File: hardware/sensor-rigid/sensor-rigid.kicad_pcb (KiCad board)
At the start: 4 copper layers, 28.5 x 21.7 mm, 27 parts, among them J1 Conn_01x05, U1 PCA9546APWR

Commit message: Interrupts and new flex design
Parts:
- moved R7 8.97 mm to (156.8, 51.8)
- moved R3 7.17 mm to (154.0, 54.2), turned to 180 degrees
- moved R13 7.07 mm to (160.5, 61.5)
- moved R9 7.00 mm to (160.8, 51.6), turned to 0 degrees
- moved JP4 6.35 mm to (163.1, 60.9)
- moved JP3 3.54 mm to (163.2, 58.4)
- moved R14 3.54 mm to (160.6, 58.5)
- moved R6 2.92 mm to (153.6, 51.8), turned to 0 degrees
- moved TP4 2.66 mm to (147.8, 63.8)
- moved R12 2.63 mm to (150.2, 61.4), turned to -90 degrees
- moved D1 2.26 mm to (139.6, 44.9)
- moved R4 2.26 mm to (138.8, 47.2)
- moved TP3 2.15 mm to (148.0, 57.8)
- moved R2 1.86 mm to (146.2, 60.6)
- moved U1 1.42 mm to (153.9, 58.9)
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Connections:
- net Net-(U1-SD0) renamed /SDA1
- net Net-(U1-SD1) renamed /SDA2
- D2 pad 3: Net-(D2-COM) -> /INT1
- D3 pad 3: Net-(D3-COM) -> /INT2
- FPC1 pad 2: Net-(D2-COM) -> /SCL1
- FPC1 pad 4: Net-(U1-SC0) -> /INT1
- FPC1 pad 6: Net-(D3-COM) -> /SCL2
- FPC1 pad 8: Net-(U1-SC1) -> /INT2
- R7 pad 2: Net-(U1-SC1) -> /SCL2
- R9 pad 1: Net-(U1-SC0) -> /SCL1
- U1 pad 5: Net-(U1-SC0) -> /SCL1
- U1 pad 7: Net-(U1-SC1) -> /SCL2
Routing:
- net Net-(D2-COM): track 18.9 -> 0.00 mm
- net /INT1: track 0.00 -> 17.3 mm
- net /SCL2: track 0.00 -> 14.9 mm
- net /SCL1: track 0.00 -> 14.7 mm
- net Net-(U1-SC1): track 13.5 -> 0.00 mm
- net Net-(D3-COM): track 10.8 -> 0.00 mm
- net /INT2: track 0.00 -> 9.85 mm
- net Net-(U1-SC0): track 9.59 -> 0.00 mm
- net Net-(JP4-A): track 4.70 -> 12.1 mm, vias 0 -> 2
- net /SDA2: track 10.3 -> 16.0 mm
- net Net-(U1-~{RESET}): track 6.19 -> 1.82 mm
- net +3.3V: track 24.5 -> 20.9 mm, vias 17 -> 14
- net Net-(JP3-A): track 6.37 -> 9.45 mm, vias 0 -> 2
- net Net-(U1-A2): track 1.98 -> 4.92 mm
- net /SDA1: track 10.5 -> 12.3 mm
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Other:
- board size 28.5 x 21.7 mm -> 28.5 x 22.7 mm
- board text added: "+3V"
- board text added: "A0"
- board text added: "A1"
- board text added: "GND"
- board text added: "INT2"
- board text removed: "3.3v"

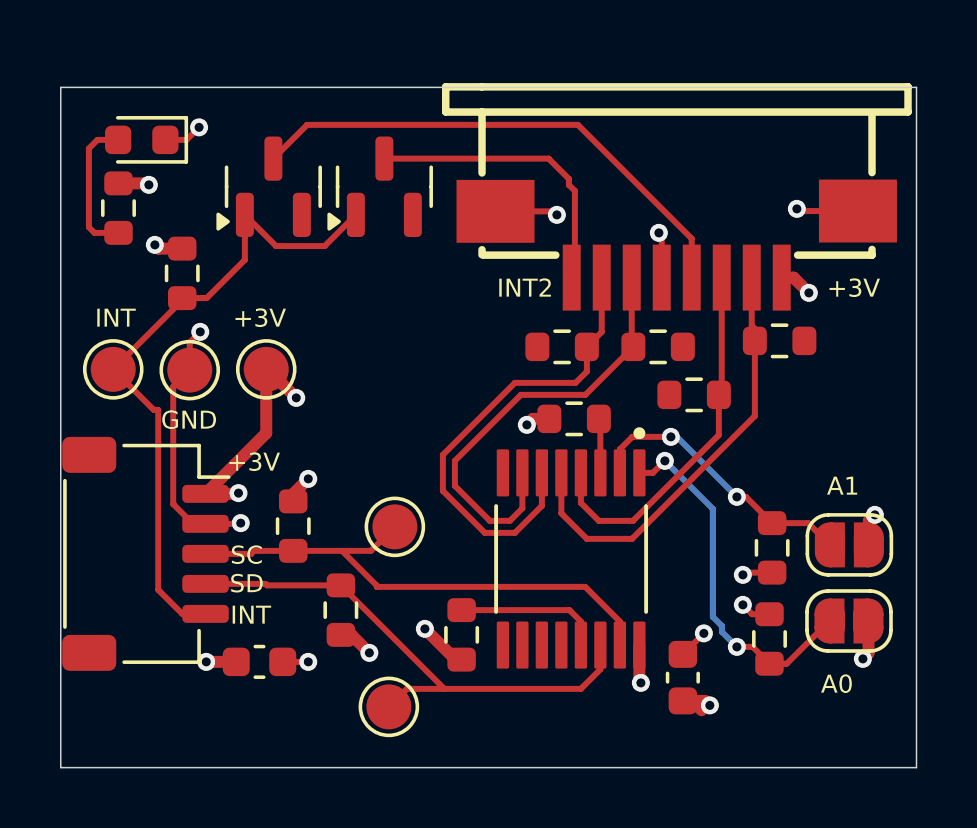
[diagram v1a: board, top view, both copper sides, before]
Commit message: Fixed calibration button on the frontend, now it shows
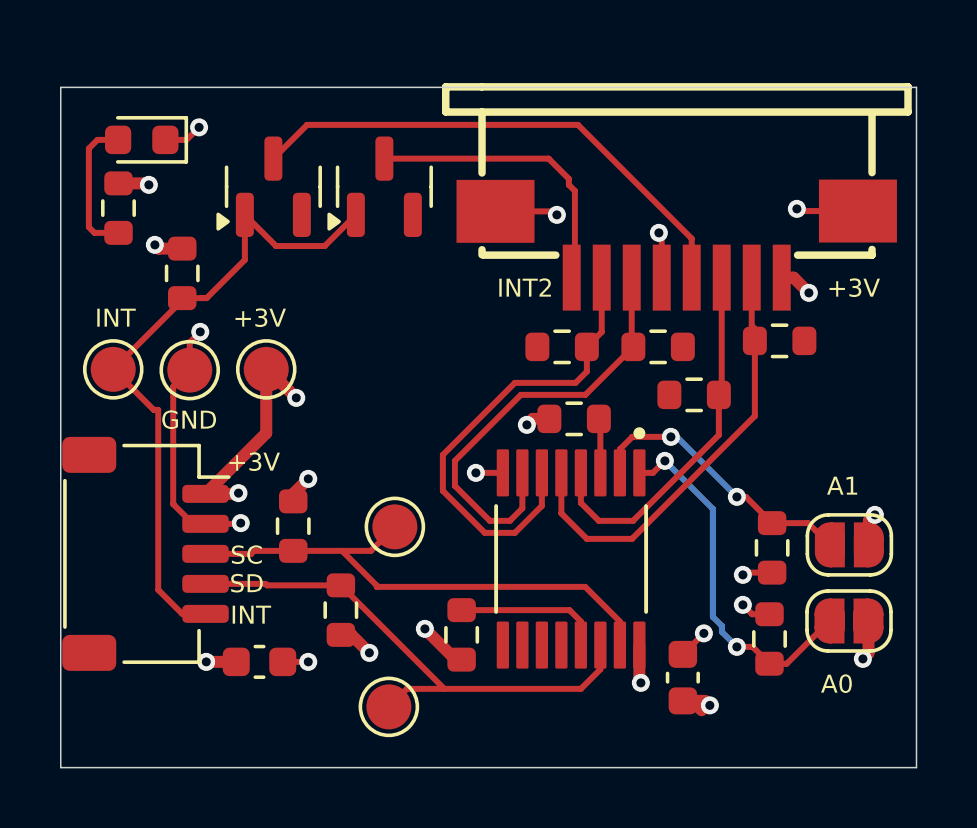
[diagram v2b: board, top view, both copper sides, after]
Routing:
- net GND: track 19.5 -> 20.4 mm, vias 10 -> 11
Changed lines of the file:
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@@
+	)
+	(segment
+		(start 151.6 56)
+		(end 150.7 56)
+		(width 0.2)
+		(layer "F.Cu")
+		(net 2)
 	)
 	(segment
@@
 		(size 0.6)
 		(drill 0.3)
+		(layers "F.Cu" "B.Cu")
+		(net 2)
+	)
+	(via
+		(at 150.7 56)
+		(size 0.6)
+		(drill 0.3)

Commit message: Hardware revision: remove interrupts, update connectors, add DIP switch
Remove INT lines from all three PCBs (main, rigid, flex). Replace 5-pin
JST-SH connectors with 4-pin SM04B-SRSS-TB on main and rigid boards.
Replace solder jumpers with EP-02KS DIP switch for I2C address config
on rigid board. Update FPC connector pinout to remove INT signals and
add GND fills. Update stiffener specs (PI 0.25mm tail, SS 0.2mm IC
areas). Regenerate production files (BOM, CPL) for both sensor boards.
Update hardware CONTEXT.md with corrected addresses (0x74-0x76),
component tables, and pinouts.

Made-with: Cursor
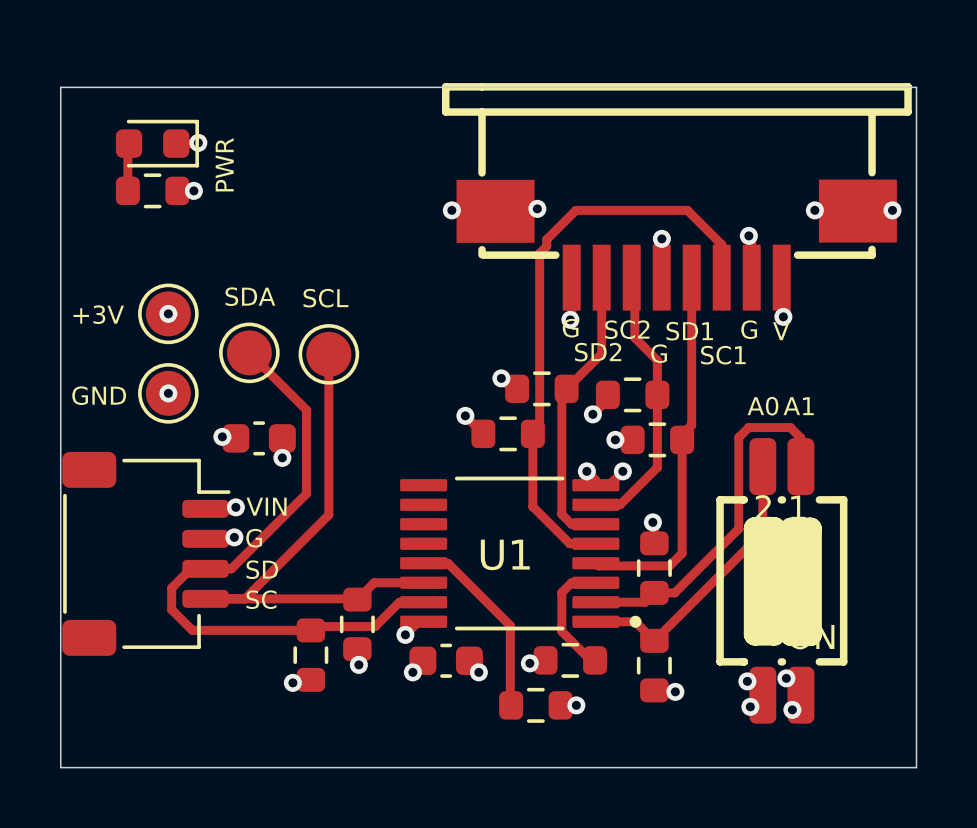
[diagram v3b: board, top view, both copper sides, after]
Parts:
- removed D2, D3: BAT54S, Package_TO_SOT_SMD:SOT-23
- removed JP3, JP4: SolderJumper_2_Open, Jumper:SolderJumper-2_P1.3mm_Open_RoundedPad1.0x1.5mm
- removed R5: 8.2kΩ, Resistor_SMD:R_0603_1608Metric
- removed TP5: TestPoint_Small, TestPoint:TestPoint_Pad_D1.5mm
- added SW1: EP-02KS, JLC-MCP:SW-SMD_EP-02KS, F.Cu at (160.9, 59.6)
- J1: value Conn_01x05 -> Conn_01x04; footprint Connector_JST:JST_SH_SM05B-SRSS-TB_1x05-1MP_P1.00mm_Horizontal -> Connector_JST:JST_SH_SM04B-SRSS-TB_1x04-1MP_P1.00mm_Horizontal
- TP1: value TestPoint_Small -> 3V3
- TP2: value TestPoint_Small -> GND
- TP3: value TestPoint_Small -> SDA_UP
- TP4: value TestPoint_Small -> SCL_UP
- moved TP4 11.9 mm to (145.8, 52.0)
- moved R9 9.57 mm to (151.8, 54.7), turned to 180 degrees
- moved R3 8.05 mm to (153.8, 62.2)
- moved C2 7.91 mm to (149.7, 62.3), turned to 180 degrees
- moved TP3 7.56 mm to (143.2, 52.0)
- moved C1 7.45 mm to (143.5, 54.9)
- moved R1 4.34 mm to (145.2, 62.1), turned to 90 degrees
- moved R14 3.98 mm to (156.7, 59.2), turned to -90 degrees
- moved R13 3.94 mm to (156.7, 62.4), turned to 90 degrees
- moved TP1 3.75 mm to (140.4, 50.7)
- moved R12 3.41 mm to (152.7, 63.8), turned to 0 degrees
- moved U1 2.05 mm to (151.8, 58.7), turned to 180 degrees
- moved R8 1.94 mm to (156.8, 54.9)
- moved R7 1.81 mm to (155.9, 53.4), turned to 0 degrees
- moved R6 1.55 mm to (152.9, 53.2)
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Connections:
- net Net-(D1-A) renamed /LED_A
- net Net-(J1-Pin_3) renamed /SDA_UP
- net Net-(J1-Pin_4) renamed /SCL_UP
- net Net-(JP3-A) renamed /PCA_A1
- net Net-(JP4-A) renamed /PCA_A0
- net Net-(U1-A2) renamed /PCA_A2
- net Net-(U1-~{RESET}) renamed /PCA_RESET
- FPC1 pad 2: /SCL1 -> GND
- FPC1 pad 3: /SDA1 -> /SCL1
- FPC1 pad 4: /INT1 -> /SDA1
- FPC1 pad 8: /INT2 -> GND
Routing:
- net Net-(D2-A): track 22.0 -> 0.00 mm
- net /INT1: track 17.3 -> 0.00 mm
- net /INT2: track 9.85 -> 0.00 mm
- net +3.3V: track 20.9 -> 12.9 mm, vias 14 -> 19
- net /SDA2: track 16.0 -> 9.72 mm
- net /SCL2: track 14.9 -> 9.25 mm
- net /SCL1: track 14.7 -> 19.5 mm
- net GND: track 20.4 -> 15.7 mm, vias 11 -> 16
- net /SDA_UP: track 17.7 -> 21.1 mm
- net /LED_A: track 4.78 -> 1.59 mm
- net /PCA_A1: track 9.45 -> 12.1 mm, vias 2 -> 0
- net /PCA_A0: track 12.1 -> 9.52 mm, vias 2 -> 0
- net /PCA_RESET: track 1.82 -> 4.07 mm
- net /PCA_A2: track 4.92 -> 6.42 mm
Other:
- board text added: "G"
- board text added: "PWR"
- board text added: "SC1"
- board text added: "SC2"
- board text added: "SCL"
- board text added: "SD1"
- board text added: "SD2"
- board text added: "SDA"
- board text added: "V"
- board text added: "VIN"
- board text removed: "INT"
- board text removed: "INT2"
